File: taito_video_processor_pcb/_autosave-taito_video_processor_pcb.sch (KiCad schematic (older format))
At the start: 342 parts, among them J1 14pin, J19 2pin, J2 14pin, J3 50pin, J6 50pin, Q1 2N3904, Q2 2N3904, Q3 2N3904, Q4 2N3904, Q5 2N3904, Q6 2N3904, Q7 2N3904, Q8 2N3905, SW1 SW_Push, U1 245_1, U10 4116, U100 LS00, U101 LS08, U102 LS10, U103 LS00, U104 157_1, U105 299_1, U106 299_1, U107 299_1, U108 299_1, U109 299_1, U11 4116, U110 299_1, U12 4116, U13 4116, U14 4116, U15 4116, U16 4116, U17 4116, U18 68A45, U19 86_2, U2 245_1, U20 86_1, U21 157_1, U22 LS32, U23 161_1, U24 LS04, U25 374_1, U26 4116, U27 4116, U28 4116, U29 4116, U3 2114, U30 4116, U31 4116, U32 4116, U33 4116, U34 LS374, U35 153_1, U36 LS74, U37 LS08, U38 74S113, U39 LS04, U4 2114, U40 7417, U41 4116, U42 4116, U43 4116, U44 4116, U45 4116, U46 4116, U47 4116, U48 4116, U49 LS32, U5 157_1, U50 86_3, U51 LS86, U52 153_1, U53 153_1, U54 153_1, U55 157_1, U56 2148_1, U57 2148_2, U58 7417, U59 4116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

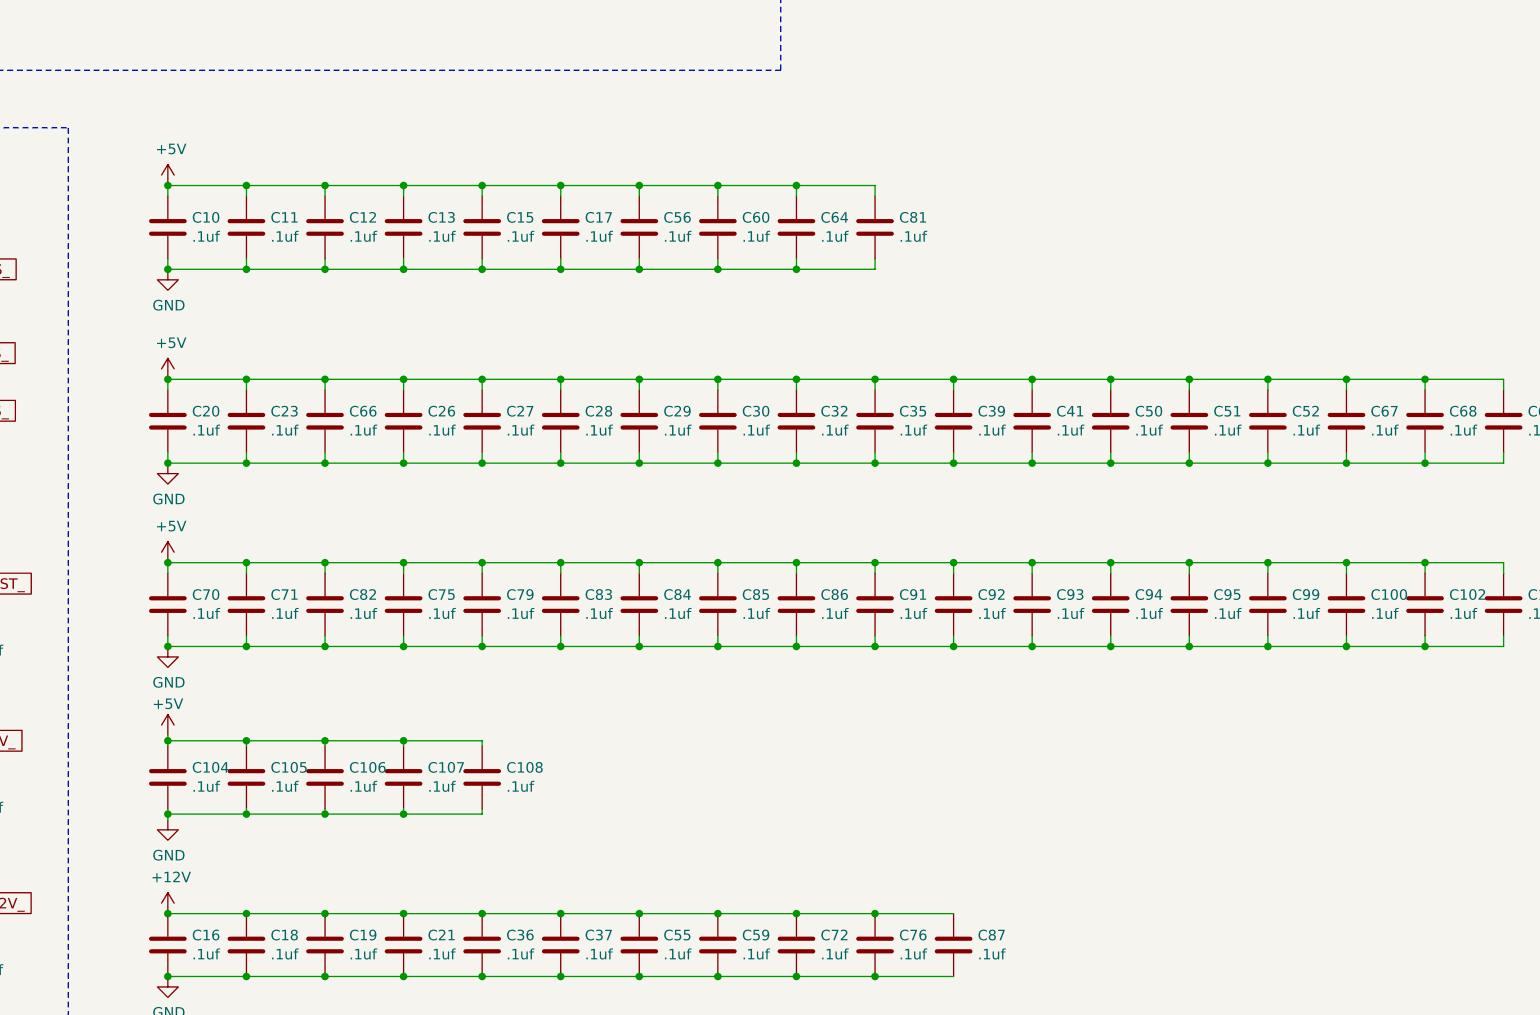
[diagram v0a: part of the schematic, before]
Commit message: Began laying down traces to figure out the best spacing and via sizes
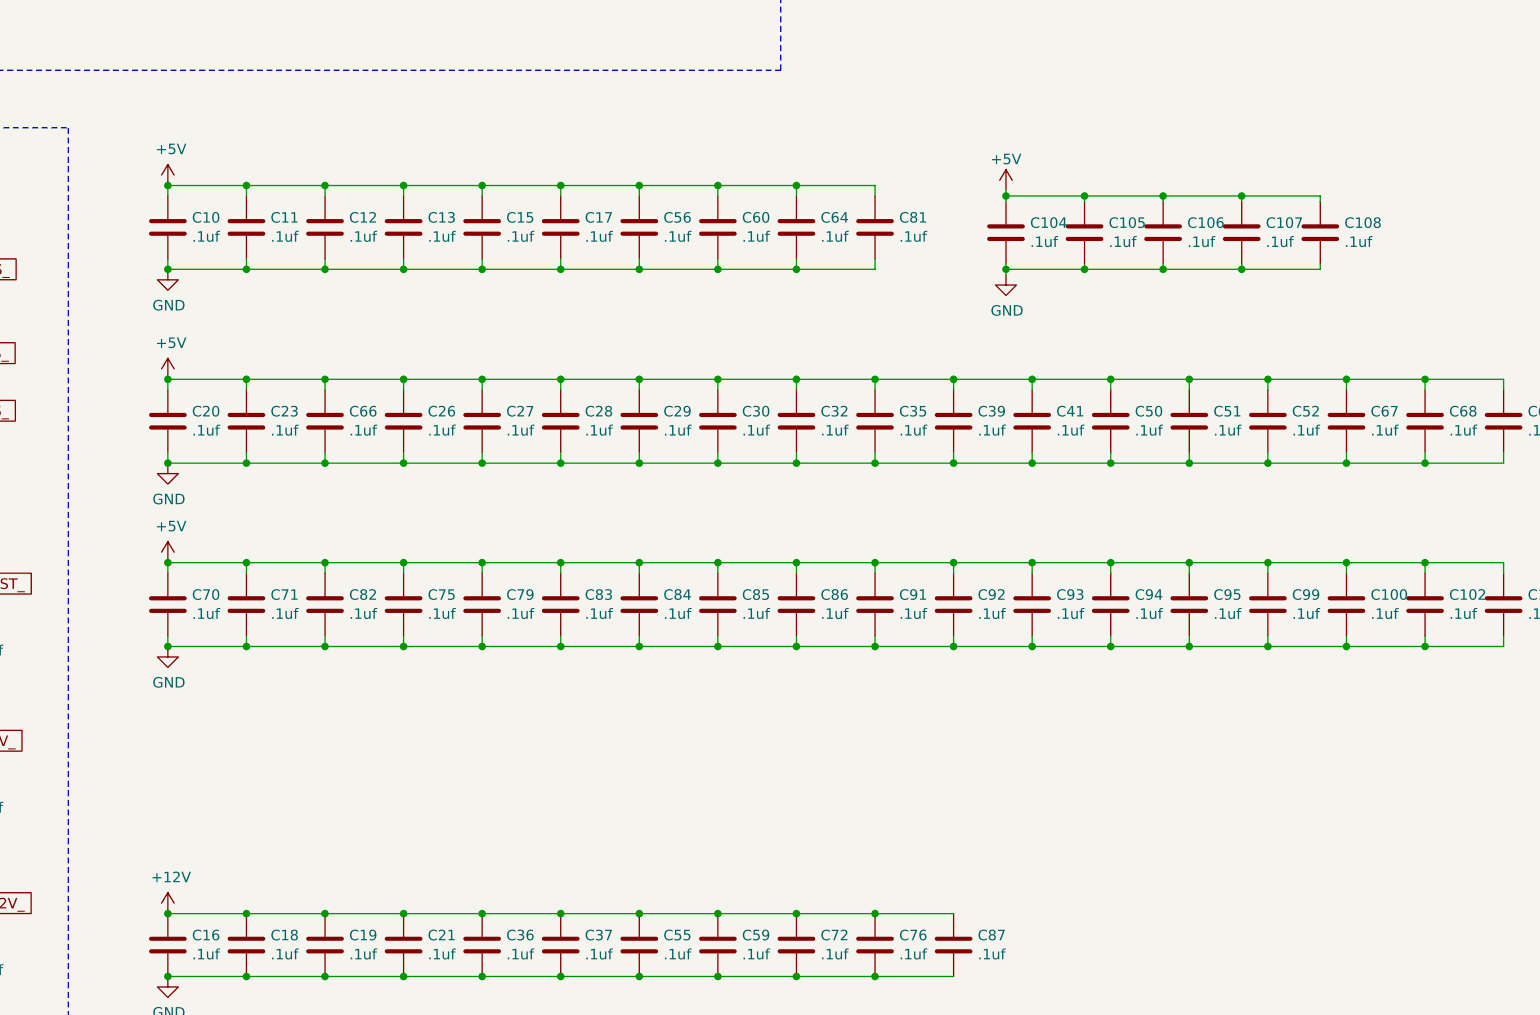
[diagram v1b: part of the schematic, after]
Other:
- moved on the sheet: C104, C105, C106, C107, C108
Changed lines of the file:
@@
 L Device:C C104
 U 1 1 9880CFE0
-P 25975 19650
-F 0 "C104" H 26090 19696 50  0000 L CNN
-F 1 ".1uf" H 26090 19605 50  0000 L CNN
-F 2 "taito_video_processor_pcb:GenericComp" H 26013 19500 50  0001 C CNN
-F 3 "~" H 25975 19650 50  0001 C CNN
-	1    25975 19650
+P 29975 17050
+F 0 "C104" H 30090 17096 50  0000 L CNN
+F 1 ".1uf" H 30090 17005 50  0000 L CNN
+F 2 "taito_video_processor_pcb:GenericComp" H 30013 16900 50  0001 C CNN
+F 3 "~" H 29975 17050 50  0001 C CNN
+	1    29975 17050
 	1    0    0    -1
 $EndComp
@@
 L Device:C C105
 U 1 1 9880D783
-P 26350 19650
-F 0 "C105" H 26465 19696 50  0000 L CNN
-F 1 ".1uf" H 26465 19605 50  0000 L CNN
-F 2 "taito_video_processor_pcb:GenericComp" H 26388 19500 50  0001 C CNN
-F 3 "~" H 26350 19650 50  0001 C CNN
-	1    26350 19650
+P 30350 17050
+F 0 "C105" H 30465 17096 50  0000 L CNN
+F 1 ".1uf" H 30465 17005 50  0000 L CNN
+F 2 "taito_video_processor_pcb:GenericComp" H 30388 16900 50  0001 C CNN
+F 3 "~" H 30350 17050 50  0001 C CNN
+	1    30350 17050
 	1    0    0    -1
 $EndComp
@@
 L Device:C C106
 U 1 1 9880DCC9
-P 26725 19650
-F 0 "C106" H 26840 19696 50  0000 L CNN
-F 1 ".1uf" H 26840 19605 50  0000 L CNN
-F 2 "taito_video_processor_pcb:GenericComp" H 26763 19500 50  0001 C CNN
-F 3 "~" H 26725 19650 50  0001 C CNN
-	1    26725 19650
+P 30725 17050
+F 0 "C106" H 30840 17096 50  0000 L CNN
+F 1 ".1uf" H 30840 17005 50  0000 L CNN
+F 2 "taito_video_processor_pcb:GenericComp" H 30763 16900 50  0001 C CNN
+F 3 "~" H 30725 17050 50  0001 C CNN
+	1    30725 17050
 	1    0    0    -1
 $EndComp
@@
 L Device:C C107
 U 1 1 9880E180
-P 27100 19650
-F 0 "C107" H 27215 19696 50  0000 L CNN
-F 1 ".1uf" H 27215 19605 50  0000 L CNN
-F 2 "taito_video_processor_pcb:GenericComp" H 27138 19500 50  0001 C CNN
-F 3 "~" H 27100 19650 50  0001 C CNN
-	1    27100 19650
+P 31100 17050
+F 0 "C107" H 31215 17096 50  0000 L CNN
+F 1 ".1uf" H 31215 17005 50  0000 L CNN
+F 2 "taito_video_processor_pcb:GenericComp" H 31138 16900 50  0001 C CNN
+F 3 "~" H 31100 17050 50  0001 C CNN
+	1    31100 17050
 	1    0    0    -1
 $EndComp
@@
 L power:GND #PWR0370
 U 1 1 9880F733
-P 25975 19850
-F 0 "#PWR0370" H 25975 19600 50  0001 C CNN
-F 1 "GND" H 25980 19677 50  0000 C CNN
-F 2 "" H 25975 19850 50  0001 C CNN
-F 3 "" H 25975 19850 50  0001 C CNN
-	1    25975 19850
+P 29975 17250
+F 0 "#PWR0370" H 29975 17000 50  0001 C CNN
+F 1 "GND" H 29980 17077 50  0000 C CNN
+F 2 "" H 29975 17250 50  0001 C CNN
+F 3 "" H 29975 17250 50  0001 C CNN
+	1    29975 17250
 	1    0    0    -1
 $EndComp
@@
 L power:+5V #PWR0371
 U 1 1 9881069E
-P 25975 19450
-F 0 "#PWR0371" H 25975 19300 50  0001 C CNN
-F 1 "+5V" H 25975 19600 50  0000 C CNN
-F 2 "" H 25975 19450 50  0001 C CNN
-F 3 "" H 25975 19450 50  0001 C CNN
-	1    25975 19450
-	1    0    0    -1
-$EndComp
-Wire Wire Line
-	25975 19450 25975 19475
-Wire Wire Line
-	25975 19475 26350 19475
-Wire Wire Line
-	26350 19475 26350 19500
-Connection ~ 25975 19475
-Wire Wire Line
-	25975 19475 25975 19500
-Wire Wire Line
-	25975 19800 25975 19825
-Wire Wire Line
-	25975 19825 26350 19825
-Wire Wire Line
-	26350 19825 26350 19800
-Connection ~ 25975 19825
-Wire Wire Line
-	25975 19825 25975 19850
-Wire Wire Line
-	27100 19500 27100 19475
-Wire Wire Line
-	27100 19475 26725 19475
-Connection ~ 26350 19475
-Wire Wire Line
-	26725 19500 26725 19475
-Connection ~ 26725 19475
-Wire Wire Line
-	26725 19475 26350 19475
-Wire Wire Line
-	26350 19825 26725 19825
-Wire Wire Line
-	27100 19825 27100 19800
-Connection ~ 26350 19825
-Wire Wire Line
-	26725 19800 26725 19825
-Connection ~ 26725 19825
-Wire Wire Line
-	26725 19825 27100 19825
+P 29975 16850
+F 0 "#PWR0371" H 29975 16700 50  0001 C CNN
+F 1 "+5V" H 29975 17000 50  0000 C CNN
+F 2 "" H 29975 16850 50  0001 C CNN
+F 3 "" H 29975 16850 50  0001 C CNN
+	1    29975 16850
+	1    0    0    -1
+$EndComp
+Wire Wire Line
+	29975 16850 29975 16875
+Wire Wire Line
+	29975 16875 30350 16875
+Wire Wire Line
+	30350 16875 30350 16900
+Connection ~ 29975 16875
+Wire Wire Line
+	29975 16875 29975 16900
+Wire Wire Line
+	29975 17200 29975 17225
+Wire Wire Line
+	29975 17225 30350 17225
+Wire Wire Line
+	30350 17225 30350 17200
+Connection ~ 29975 17225
+Wire Wire Line
+	29975 17225 29975 17250
+Wire Wire Line
+	31100 16900 31100 16875
+Wire Wire Line
+	31100 16875 30725 16875
+Connection ~ 30350 16875
+Wire Wire Line
+	30725 16900 30725 16875
+Connection ~ 30725 16875
+Wire Wire Line
+	30725 16875 30350 16875
+Wire Wire Line
+	30350 17225 30725 17225
+Wire Wire Line
+	31100 17225 31100 17200
+Connection ~ 30350 17225
+Wire Wire Line
+	30725 17200 30725 17225
+Connection ~ 30725 17225
+Wire Wire Line
+	30725 17225 31100 17225
 Wire Wire Line
 	29350 18625 29725 18625
@@
 L Device:C C108
 U 1 1 9F823FC4
-P 27475 19650
-F 0 "C108" H 27590 19696 50  0000 L CNN
-F 1 ".1uf" H 27590 19605 50  0000 L CNN
-F 2 "taito_video_processor_pcb:GenericComp" H 27513 19500 50  0001 C CNN
-F 3 "~" H 27475 19650 50  0001 C CNN
-	1    27475 19650
-	1    0    0    -1
-$EndComp
-Wire Wire Line
-	27475 19500 27475 19475
-Wire Wire Line
-	27475 19475 27100 19475
-Connection ~ 27100 19475
-Wire Wire Line
-	27475 19800 27475 19825
-Wire Wire Line
-	27475 19825 27100 19825
-Connection ~ 27100 19825
+P 31475 17050
+F 0 "C108" H 31590 17096 50  0000 L CNN
+F 1 ".1uf" H 31590 17005 50  0000 L CNN
+F 2 "taito_video_processor_pcb:GenericComp" H 31513 16900 50  0001 C CNN
+F 3 "~" H 31475 17050 50  0001 C CNN
+	1    31475 17050
+	1    0    0    -1
+$EndComp
+Wire Wire Line
+	31475 16900 31475 16875
+Wire Wire Line
+	31475 16875 31100 16875
+Connection ~ 31100 16875
+Wire Wire Line
+	31475 17200 31475 17225
+Wire Wire Line
+	31475 17225 31100 17225
+Connection ~ 31100 17225
 Wire Wire Line
 	24925 21975 24925 22025
